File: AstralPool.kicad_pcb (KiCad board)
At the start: 2 copper layers, 80 x 75 mm, 23 parts, among them J1 RJ12, J2 RJ12, J3 Header, J4 Conn_02x12_Counter_Clockwise, Q1 2N3904, U1 LM2678T-5.0/NOPB

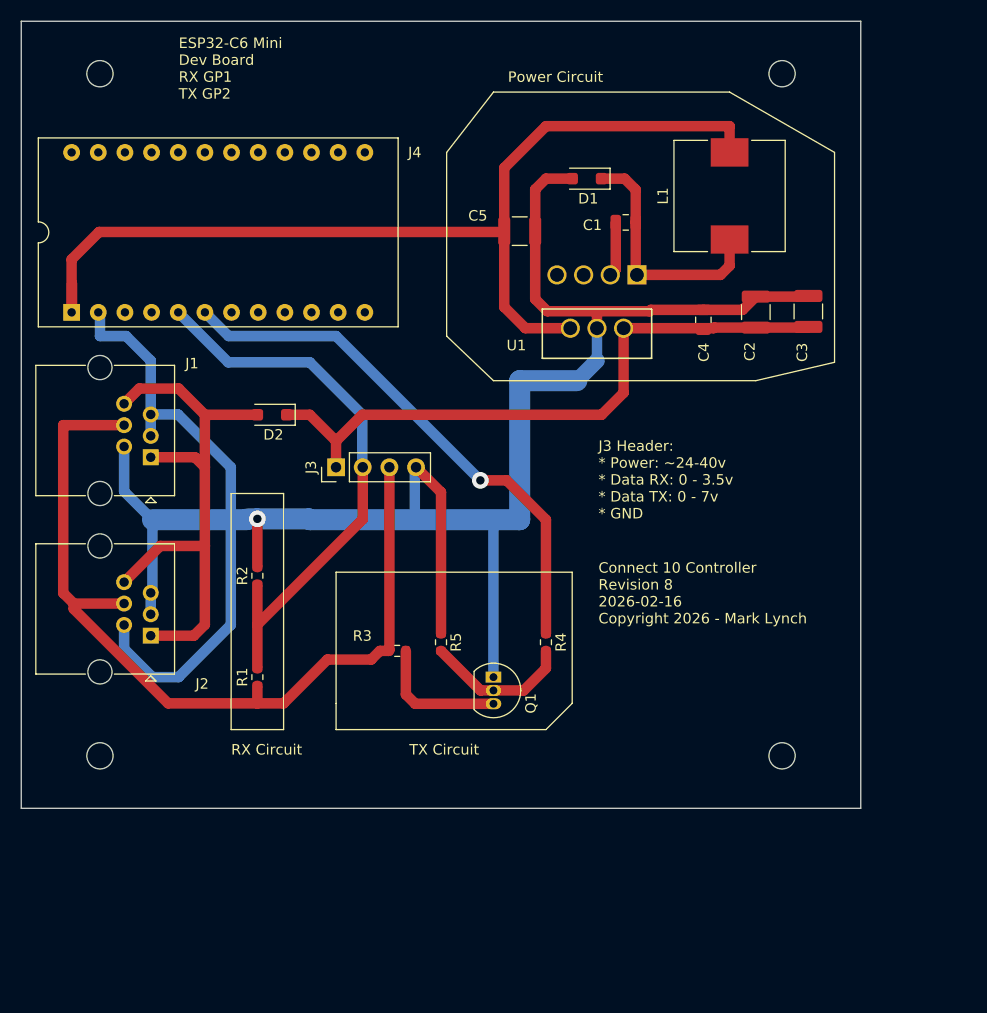
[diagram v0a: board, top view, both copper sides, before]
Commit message: ### Changed - Rev 9 - Moved the power buck to surface mount component LM2678S-5.0/NOPB - Rev 9 - Moved the transistor to a SMD - Rev 9 - Added copper pour for GND on both sides - Rev 9 - Tided up annotations
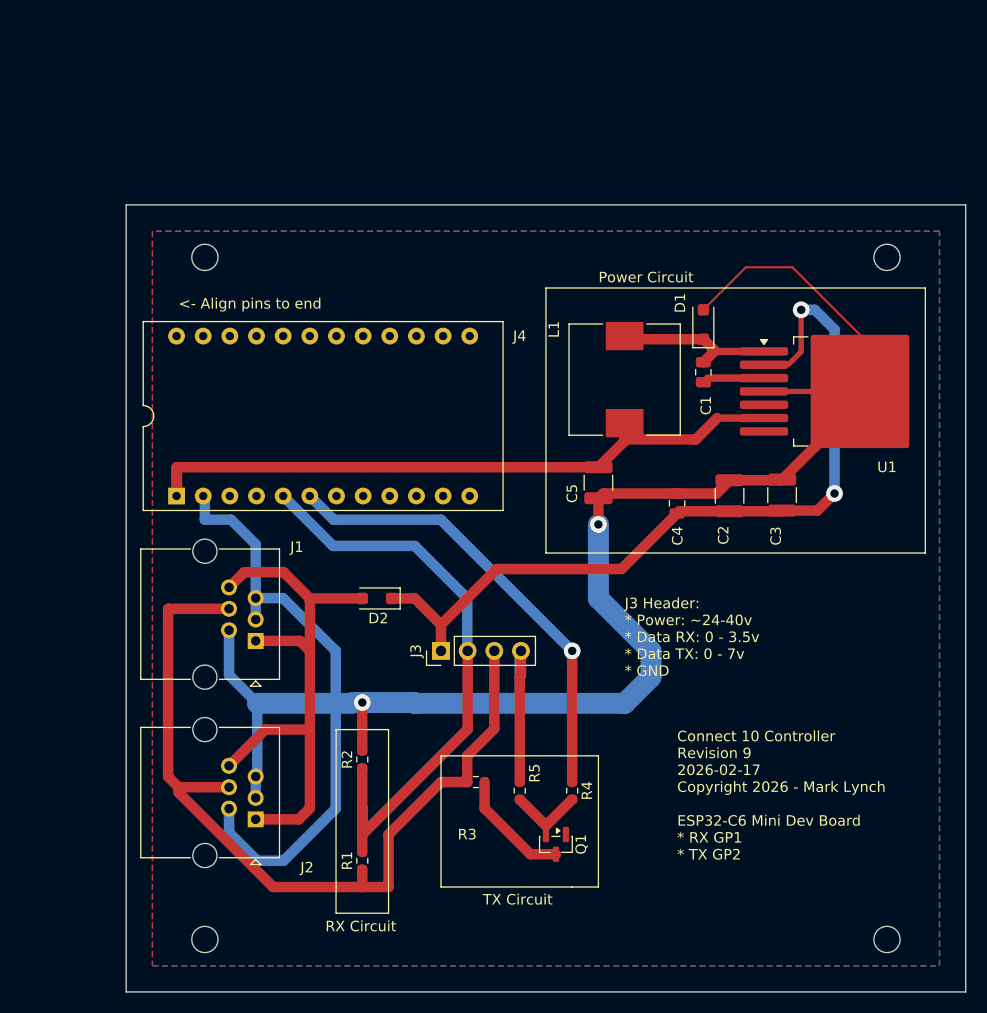
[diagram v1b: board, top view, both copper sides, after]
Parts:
- Q1: value 2N3904 -> MMBT3904; footprint Package_TO_SOT_THT:TO-92_Inline -> Package_TO_SOT_SMD:SOT-23
- U1: value LM2678T-5.0/NOPB -> LM2678S-5.0/NOPB; footprint TA07B:TA07B -> Package_TO_SOT_SMD:TO-263-7_TabPin4
- moved U1 27.4 mm to (133.4, 57.8), turned to 0 degrees
- moved C5 25.1 mm to (110.0, 66.5), turned to -90 degrees
- moved D2 20.2 mm to (88.9, 77.5)
- moved J1 20.2 mm to (77.3, 81.5)
- moved J2 20.2 mm to (77.3, 98.5)
- moved J3 20.2 mm to (95.0, 82.5)
- moved L1 20.2 mm to (112.5, 56.6), turned to -90 degrees
- moved R1 20.2 mm to (87.5, 102.5)
- moved R2 20.2 mm to (87.5, 92.8)
- moved REF** 20.2 mm to (72.5, 45.0)
- moved REF** 20.2 mm to (137.5, 45.0)
- moved REF** 20.2 mm to (137.5, 110.0)
- moved REF** 20.2 mm to (72.5, 110.0)
- moved J4 20.2 mm to (69.8, 67.7)
- moved D1 17.8 mm to (120.0, 51.4), turned to 90 degrees
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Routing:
- net +5V (from buck power): track 96.1 -> 67.5 mm
- net Net-(D2-K): track 61.3 -> 78.5 mm, vias 0 -> 2
- net Net-(D1-K): track 23.5 -> 15.4 mm
- net Net-(J4-Pin_6): track 51.5 -> 43.6 mm
- net Net-(Q1-B): track 14.1 -> 6.94 mm
- net Net-(J3-Pin_2): track 53.8 -> 58.8 mm
- net GND (from connector): track 217.0 -> 220.6 mm, vias 1 -> 2
- net Net-(Q1-C): track 12.9 -> 11.1 mm
- net Net-(J3-Pin_3): track 83.5 -> 82.1 mm
- net Net-(U1-CB): track 5.22 -> 5.94 mm
- added copper zone on B.Cu, net GND (from connector)
- added copper zone on F.Cu, net GND (from connector)
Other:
- board text added: "${TITLE} ${REVISION} ${ISSUE_DATE} ${COMPANY} ESP32-C6 Mini Dev Board * RX GP1 * TX GP2"
- board text added: "<- Align pins to end"
- board text removed: "${TITLE} ${REVISION} ${ISSUE_DATE} ${COMPANY}"
- board text removed: "ESP32-C6 Mini Dev Board RX GP1 TX GP2"

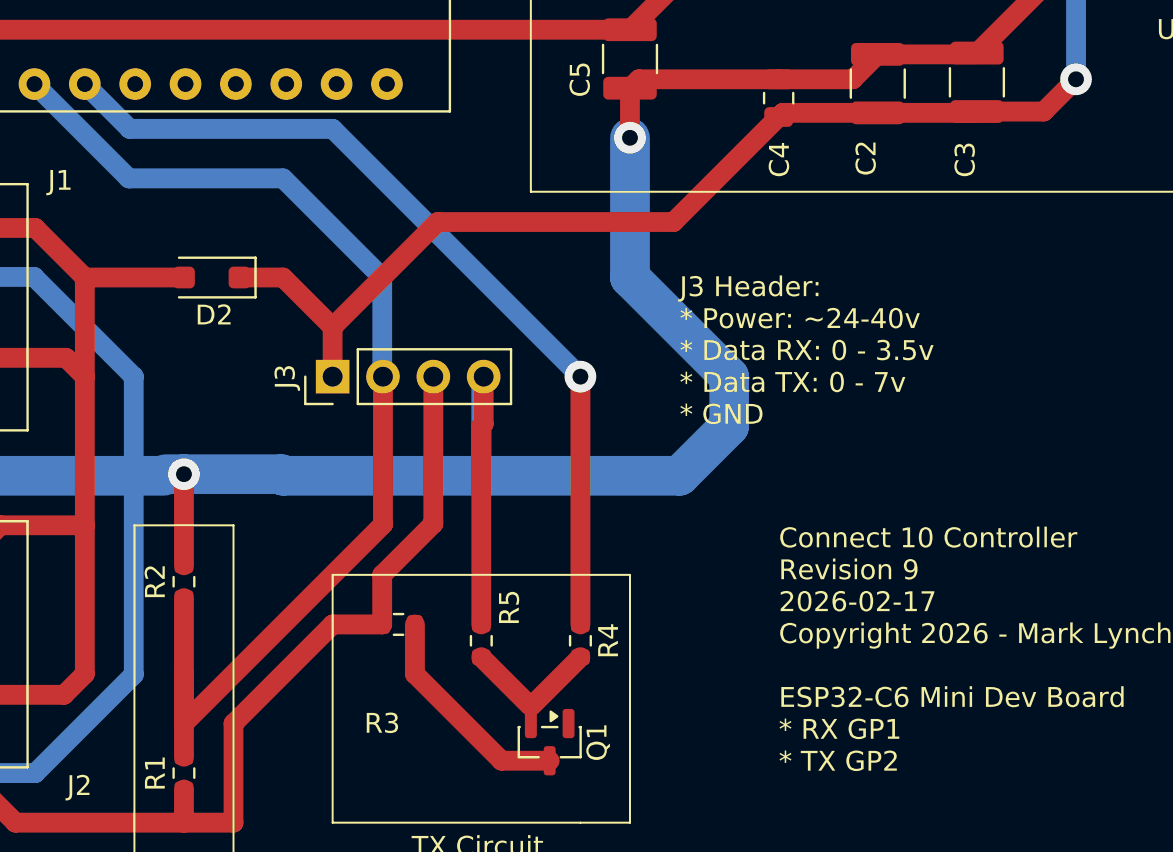
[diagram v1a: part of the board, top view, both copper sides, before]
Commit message: ### Changed - Rev 9 - Reorient header and move labelling closer
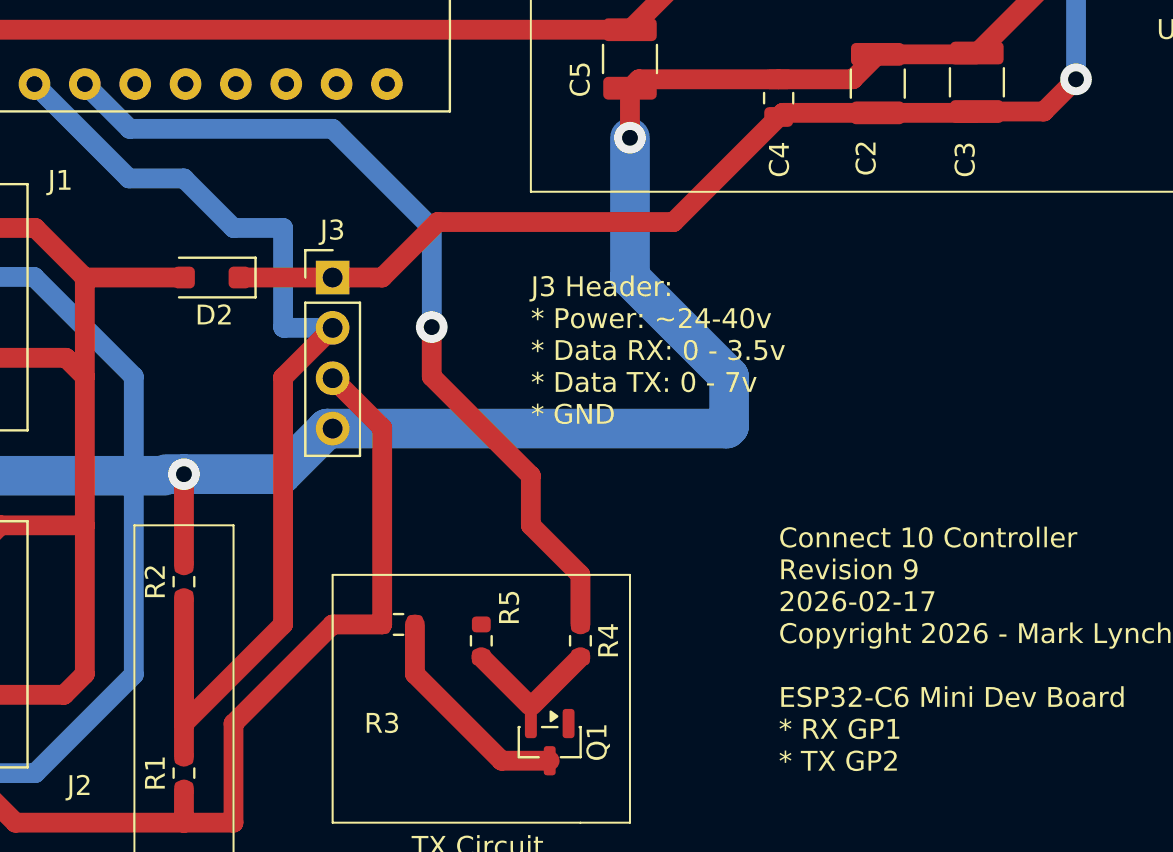
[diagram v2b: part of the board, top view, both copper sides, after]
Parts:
- moved J3 5.00 mm to (95.0, 77.5), turned to 0 degrees
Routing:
- net GND (from connector): track 220.6 -> 202.9 mm
- net Net-(D2-K): track 78.5 -> 74.0 mm
- net Net-(J3-Pin_2): track 58.8 -> 56.6 mm

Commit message: ### Changed - Rev 10 - moved C5 closer to U1 - Rev 10 - added via under U1 - Rev 10 - minor layout improvements.
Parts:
- D1, D2: value D 6TQ045S -> PMEG6010CEH,115
- moved C5 10.1 mm to (120.0, 65.0)
- moved C3 2.35 mm to (127.5, 70.0)
- moved C2 2.28 mm to (122.5, 70.0)
- moved C4 1.55 mm to (117.5, 70.0)
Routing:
- net GND (from connector): track 202.9 -> 206.5 mm, vias 2 -> 3
- net +5V (from buck power): track 67.5 -> 69.4 mm
- net Net-(D2-K): track 74.0 -> 75.9 mm
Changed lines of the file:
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@@
 	(title_block
 		(title "Connect 10 Controller")
-		(date "2026-02-17")
-		(rev "Revision 9")
+		(date "2026-02-18")
+		(rev "Revision 10")
 		(company "Copyright 2026 - Mark Lynch")
 	)
@@
 	(footprint "Capacitor_SMD:C_0805_2012Metric"
 		(layer "F.Cu")
-		(at 117.5 68.45 90)
+		(at 117.5 70 90)
 		(descr "Capacitor SMD 0805 (2012 Metric), square (rectangular) end terminal, IPC-7351 nominal, (Body size source: IPC-SM-782 page 76, https://www.pcb-3d.com/wordpress/wp-content/uploads/ipc-sm-782a_amendment_1_and_2.pdf, https://docs.google.com/spreadsheets/d/1BsfQQcO9C6DZCsRaXUlFlo91Tg2WpOkGARC1WS5S8t0/edit?usp=sharing), generated with kicad-footprint-generator")
 		(tags "capacitor")
@@
 	(footprint "Capacitor_SMD:C_1210_3225Metric"
 		(layer "F.Cu")
-		(at 122.5 67.717653 90)
+		(at 122.5 70 90)
 		(descr "Capacitor SMD 1210 (3225 Metric), square (rectangular) end terminal, IPC-7351 nominal, (Body size source: IPC-SM-782 page 76, https://www.pcb-3d.com/wordpress/wp-content/uploads/ipc-sm-782a_amendment_1_and_2.pdf), generated with kicad-footprint-generator")
 		(tags "capacitor")
@@
 			)
 		)
-		(property "Value" "D 6TQ045S"
+		(property "Value" "PMEG6010CEH,115"
 			(at 0 2.1 0)
 			(layer "F.Fab")
@@
 	(footprint "Capacitor_SMD:C_1210_3225Metric"
 		(layer "F.Cu")
-		(at 110 66.475 -90)
+		(at 120 65 -90)
 		(descr "Capacitor SMD 1210 (3225 Metric), square (rectangular) end terminal, IPC-7351 nominal, (Body size source: IPC-SM-782 page 76, https://www.pcb-3d.com/wordpress/wp-content/uploads/ipc-sm-782a_amendment_1_and_2.pdf), generated with kicad-footprint-generator")
 		(tags "capacitor")
@@
 			)
 		)
-		(property "Value" "D 6TQ045S"
+		(property "Value" "PMEG6010CEH,115"
 			(at 0 2.1 90)
 			(layer "F.Fab")
@@
 	(footprint "Capacitor_SMD:C_1210_3225Metric"
 		(layer "F.Cu")
-		(at 127.5 67.65177 90)
+		(at 127.5 70 90)
 		(descr "Capacitor SMD 1210 (3225 Metric), square (rectangular) end terminal, IPC-7351 nominal, (Body size source: IPC-SM-782 page 76, https://www.pcb-3d.com/wordpress/wp-content/uploads/ipc-sm-782a_amendment_1_and_2.pdf), generated with kicad-footprint-generator")
 		(tags "capacitor")
@@
 	(gr_poly
 		(pts
-			(xy 95 92.5) (xy 95 105) (xy 95 105) (xy 107.5 105) (xy 110 105) (xy 110 92.5)
+			(xy 95 92.5) (xy 95 105) (xy 107.5 105) (xy 110 105) (xy 110 92.5)
 		)
 		(stroke
@@
 	(gr_rect
 		(start 105 47.92031)
-		(end 141.152602 73.172808)
+		(end 141.152602 75.672808)
 		(stroke
 			(width 0.1)
@@
 		(start 120.395 56.505)
 		(end 119.999999 56.900001)
-		(width 0.5)
+		(width 0.7)
 		(layer "F.Cu")
 		(net 1)
@@
 	)
 	(segment
-		(start 127.434117 66.242653)
-		(end 127.5 66.17677)
+		(start 120 68.525)
+		(end 120 66.475)
 		(width 1)
 		(layer "F.Cu")
@@
 	)
 	(segment
-		(start 117.5 67.5)
-		(end 121.242653 67.5)
+		(start 113.975 68.525)
+		(end 112.05 70.45)
 		(width 1)
 		(layer "F.Cu")
@@
 	)
 	(segment
-		(start 122.5 66.242653)
-		(end 127.434117 66.242653)
-		(width 1)
-		(layer "F.Cu")
-		(net 6)
-	)
-	(segment
 		(start 124.05705 45.94295)
 		(end 128.49295 45.94295)
@@
 	)
 	(segment
-		(start 87.5 92.02)
-		(end 87.5 87.5)
+		(start 116.975 68.525)
+		(end 113.975 68.525)
 		(width 1)
 		(layer "F.Cu")
@@
 	)
 	(segment
-		(start 110.45 67.5)
-		(end 110 67.95)
+		(start 87.5 92.02)
+		(end 87.5 87.5)
 		(width 1)
 		(layer "F.Cu")
@@
 	)
 	(segment
-		(start 117.5 67.5)
-		(end 110.45 67.5)
-		(width 1)
-		(layer "F.Cu")
-		(net 6)
-	)
-	(segment
 		(start 134.925 52.375)
 		(end 134.925 57.775)
@@
 	)
 	(segment
-		(start 121.242653 67.5)
-		(end 122.5 66.242653)
+		(start 130 63.67677)
+		(end 130 67.5)
 		(width 1)
 		(layer "F.Cu")
@@
 	)
 	(segment
-		(start 127.5 66.17677)
-		(end 130.588385 63.088385)
+		(start 130.588385 63.088385)
+		(end 130 63.67677)
 		(width 1)
 		(layer "F.Cu")
@@
 	)
 	(segment
-		(start 110 67.95)
+		(start 128.975 68.525)
+		(end 120 68.525)
+		(width 1)
+		(layer "F.Cu")
+		(net 6)
+	)
+	(segment
+		(start 112.05 70.45)
 		(end 110 70.45)
 		(width 1)
@@
 	)
 	(segment
+		(start 120 68.525)
+		(end 116.975 68.525)
+		(width 1)
+		(layer "F.Cu")
+		(net 6)
+	)
+	(segment
+		(start 130 67.5)
+		(end 128.975 68.525)
+		(width 1)
+		(layer "F.Cu")
+		(net 6)
+	)
+	(segment
 		(start 125.775 57.775)
 		(end 130.588385 57.775)
@@
 		(net 6)
 	)
+	(segment
+		(start 117.5 69.05)
+		(end 116.975 68.525)
+		(width 1)
+		(layer "F.Cu")
+		(net 6)
+	)
+	(via
+		(at 134.924998 57.774999)
+		(size 1.6)
+		(drill 0.8)
+		(layers "F.Cu" "B.Cu")
+		(free yes)
+		(net 6)
+	)
 	(via
 		(at 110 70.45)
@@
 	)
 	(segment
+		(start 120 61.626346)
+		(end 120 63.525)
+		(width 1)
+		(layer "F.Cu")
+		(net 9)
+	)
+	(segment
 		(start 69.8 67.74)
 		(end 69.8 65.040002)
@@
 	)
 	(segment
-		(start 121.311346 60.315)
-		(end 119.276346 62.35)
+		(start 119.956652 63.481652)
+		(end 113.481652 63.481652)
 		(width 1)
 		(layer "F.Cu")
@@
 	)
 	(segment
-		(start 112.65 62.35)
-		(end 112.5 62.5)
+		(start 121.311346 60.315)
+		(end 120 61.626346)
 		(width 1)
 		(layer "F.Cu")
@@
 	)
 	(segment
-		(start 119.276346 62.35)
-		(end 112.65 62.35)
+		(start 69.8 67.74)
+		(end 69.84 67.7)
 		(width 1)
 		(layer "F.Cu")
@@
 	)
 	(segment
-		(start 69.8 67.74)
-		(end 69.84 67.7)
+		(start 113.481652 63.481652)
+		(end 112.5 62.5)
 		(width 1)
 		(layer "F.Cu")
@@
 	)
 	(segment
-		(start 100.3 74.7)
-		(end 112.2 74.7)
+		(start 120 63.525)
+		(end 119.956652 63.481652)
+		(width 1)
+		(layer "F.Cu")
+		(net 9)
+	)
+	(segment
+		(start 112.2 74.7)
+		(end 100.3 74.7)
 		(width 1)
 		(layer "F.Cu")
@@
 	)
 	(segment
-		(start 95 77.5)
-		(end 97.5 77.5)
+		(start 115.95 70.95)
+		(end 112.2 74.7)
 		(width 1)
 		(layer "F.Cu")
@@
 	)
 	(segment
-		(start 122.5 69.192653)
-		(end 117.707347 69.192653)
+		(start 127.5 71.475)
+		(end 122.326844 71.475)
 		(width 1)
 		(layer "F.Cu")
@@
 	)
 	(segment
-		(start 127.434117 69.192653)
-		(end 127.5 69.12677)
-		(width 1)
+		(start 125.775 55.235)
+		(end 128.075 55.235)
+		(width 0.2)
 		(layer "F.Cu")
 		(net 10)
 	)
 	(segment
-		(start 127.5 69.12677)
-		(end 130.87323 69.12677)
+		(start 97.5 77.5)
+		(end 95 77.5)
 		(width 1)
 		(layer "F.Cu")
@@
 	)
 	(segment
-		(start 125.775 55.235)
-		(end 128.075 55.235)
-		(width 0.2)
+		(start 128.075 55.235)
+		(end 129.322622 53.987378)
+		(width 0.5)
 		(layer "F.Cu")
 		(net 10)
 	)
 	(segment
-		(start 128.075 55.235)
-		(end 129.322622 53.987378)
-		(width 0.5)
+		(start 119.575 71.475)
+		(end 119.05 70.95)
+		(width 1)
 		(layer "F.Cu")
 		(net 10)
 	)
 	(segment
-		(start 97.5 77.5)
-		(end 100.3 74.7)
+		(start 100.3 74.7)
+		(end 97.5 77.5)
 		(width 1)
 		(layer "F.Cu")
@@
 	)
 	(segment
-		(start 117.707347 69.192653)
-		(end 117.5 69.4)
+		(start 131.025 71.475)
+		(end 132.5 70)
 		(width 1)
 		(layer "F.Cu")
@@
 	)
 	(segment
-		(start 112.2 74.7)
-		(end 117.5 69.4)
+		(start 122.326844 71.475)
+		(end 119.575 71.475)
 		(width 1)
 		(layer "F.Cu")
@@
 	)
 	(segment
-		(start 130.87323 69.12677)
-		(end 132.5 67.5)
+		(start 127.5 71.475)
+		(end 131.025 71.475)
 		(width 1)
 		(layer "F.Cu")
@@
 	)
 	(segment
-		(start 122.5 69.192653)
-		(end 127.434117 69.192653)
+		(start 119.05 70.95)
+		(end 115.95 70.95)
+		(width 1)
+		(layer "F.Cu")
+		(net 10)
+	)
+	(segment
+		(start 132.5 70)
+		(end 132.5 67.5)
 		(width 1)
 		(layer "F.Cu")
